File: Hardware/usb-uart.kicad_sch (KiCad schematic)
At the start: 16 parts, among them J3 USB_C_Receptacle_USB2.0, U6 SC4216H, U7 LTC4411

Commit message: added jumper to change the buck converter to 8.4v
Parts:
- C23: footprint Capacitor_SMD:C_0603_1608Metric -> Capacitor_SMD:C_0402_1005Metric
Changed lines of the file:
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@@
       (effects (font (size 1.27 1.27)) (justify left))
     )
-    (property "Footprint" "Capacitor_SMD:C_0603_1608Metric" (id 2) (at 262.89 105.41 0)
+    (property "Footprint" "Capacitor_SMD:C_0402_1005Metric" (id 2) (at 262.89 105.41 0)
       (effects (font (size 1.27 1.27)) hide)
     )

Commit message: End of V1
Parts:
- added C10, C9: 0.1uF, Capacitor_SMD:C_0603_1608Metric, symbol Device:C_Small
- added C18: 4.7uF, Capacitor_SMD:C_0603_1608Metric, symbol Device:C_Small
- added C8: 1.0uF, Capacitor_SMD:C_0603_1608Metric, symbol Device:C_Small
- added R17: 4.7k, Resistor_SMD:R_0603_1608Metric, symbol Device:R_Small
- added R3: 24k, Resistor_SMD:R_0603_1608Metric, symbol Device:R_Small
- added R6: 47k, Resistor_SMD:R_0603_1608Metric, symbol Device:R_Small
- added U3: INTERFACE-CP2102-GMR(QFN28), iclr:QFN28G_0.5-5X5MM, symbol iclr:INTERFACE-CP2102-GMR(QFN28)
- C23: footprint Capacitor_SMD:C_0402_1005Metric -> Capacitor_SMD:C_0603_1608Metric
- U6: value SC4216H -> RT9025-25GSP
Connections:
- net 3.3V: now also C10.2, C18.2, C8.2, C9.2, U3.6 (VDD), U3.7 (REGIN)
- net Data+: now also U3.4 (D+)
- net Data-: now also U3.5 (D-)
- net GND: now also C10.1, C18.1, C8.1, C9.1, R6.1, U3.3 (GND)
- net VBUS: now also R3.1
- new net: R3.2, R6.2, U3.8 (VBUS)
- new net: R17.2, U3.9 (~{RST})
- new net +3V3: R17.1
- new net DTR: U3.28 (DTR)
- new net RTS: U3.24 (RTS)
- new net RXD: U3.25 (RXD)
- new net TXD: U3.26 (TXD)
- no-connect marks 5 -> 23

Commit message: mostly completed v2 schematic (pin assignments left)
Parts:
- removed C10, C9: 0.1uF, Capacitor_SMD:C_0603_1608Metric, symbol Device:C_Small
- removed C18, C23: 4.7uF, Capacitor_SMD:C_0603_1608Metric, symbol Device:C_Small
- removed C20, C25: 10uF, Capacitor_SMD:C_0603_1608Metric, symbol Device:C_Small
- removed C8: 1.0uF, Capacitor_SMD:C_0603_1608Metric, symbol Device:C_Small
- removed R17: 4.7k, Resistor_SMD:R_0603_1608Metric, symbol Device:R_Small
- removed R24: 56k, Resistor_SMD:R_0603_1608Metric, symbol Device:R_Small
- removed R25: 10k, Resistor_SMD:R_0603_1608Metric, symbol Device:R_Small
- removed R3: 24k, Resistor_SMD:R_0603_1608Metric, symbol Device:R_Small
- removed R6: 47k, Resistor_SMD:R_0603_1608Metric, symbol Device:R_Small
- removed U3: INTERFACE-CP2102-GMR(QFN28), iclr:QFN28G_0.5-5X5MM, symbol iclr:INTERFACE-CP2102-GMR(QFN28)
- removed U6: RT9025-25GSP, iclr:SOIC127P599X175-9N, symbol iclr:RT9025-25GSP
- removed U7: LTC4411, Package_TO_SOT_SMD:SOT-23-5, symbol iclr:LTC4411
- R11: renamed from R15; footprint Resistor_SMD:R_0603_1608Metric -> Resistor_SMD:R_0402_1005Metric
- R12: renamed from R16; footprint Resistor_SMD:R_0603_1608Metric -> Resistor_SMD:R_0402_1005Metric
- R13: renamed from R18; footprint Resistor_SMD:R_0603_1608Metric -> Resistor_SMD:R_0402_1005Metric
- USBLED1: footprint LED_SMD:LED_0603_1608Metric -> Resistor_SMD:R_0402_1005Metric
- renumbered D4 to D2, J3 to J5, TP17 to TP1, TP18 to TP2, TP19 to TP3
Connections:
- no-connect marks 23 -> 2

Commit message: Mostly completed RBUS side, still buck converter side to do
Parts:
- removed TP3: TestPoint, TestPoint:TestPoint_Pad_D1.0mm, symbol Connector:TestPoint
- USBLED1: footprint Resistor_SMD:R_0402_1005Metric -> LED_SMD:LED_0402_1005Metric
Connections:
- net Data+: now also D2.2 (K); no longer D2.4 (K)
- net VBUS: now also D2.4 (K); no longer D2.2 (K)
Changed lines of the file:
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@@
-    (stroke (width 0) (type default) (color 0 0 0 0))
-  )
-  (wire (pts (xy 44.45 109.22) (xy 52.07 109.22))
     (stroke (width 0) (type default) (color 0 0 0 0))
   )
@@
     (stroke (width 0) (type default) (color 0 0 0 0))
   )
-  (label "Data+" (at 134.62 134.62 90)
-    (effects (font (size 1.27 1.27)) (justify left bottom))
-  )
-  (label "VBUS" (at 129.54 134.62 90)
+  (label "Data+" (at 129.54 134.62 90)
     (effects (font (size 1.27 1.27)) (justify left bottom))
   )
@@
     (effects (font (size 1.27 1.27)) (justify left bottom))
   )
+  (label "Data-" (at 132.08 134.62 90)
+    (effects (font (size 1.27 1.27)) (justify left bottom))
+  )
   (label "Data-" (at 44.45 99.06 0)
     (effects (font (size 1.27 1.27)) (justify left bottom))
   )
-  (label "Data-" (at 132.08 134.62 90)
-    (effects (font (size 1.27 1.27)) (justify left bottom))
-  )
   (label "Data-" (at 116.84 102.87 0)
     (effects (font (size 1.27 1.27)) (justify left bottom))
   )
-  (label "VBUS" (at 44.45 109.22 0)
-    (effects (font (size 1.27 1.27)) (justify left bottom))
-  )
   (label "Data+" (at 116.84 107.95 0)
+    (effects (font (size 1.27 1.27)) (justify left bottom))
+  )
+  (label "VBUS" (at 134.62 134.62 90)
     (effects (font (size 1.27 1.27)) (justify left bottom))
   )
@@
     (pin "1")
   )
-  (symbol (lib_id "Connector:TestPoint") (at 52.07 109.22 270) (unit 1)
-    (in_bom yes) (on_board yes)
-    (property "Reference" "TP3" (id 0) (at 56.8452 108.0516 90)
-      (effects (font (size 1.27 1.27)) (justify left))
-    )
-    (property "Value" "TestPoint" (id 1) (at 56.8452 110.363 90)
-      (effects (font (size 1.27 1.27)) (justify left))
-    )
-    (property "Footprint" "TestPoint:TestPoint_Pad_D1.0mm" (id 2) (at 52.07 114.3 0)
-      (effects (font (size 1.27 1.27)) hide)
-    )
-    (property "Datasheet" "~" (id 3) (at 52.07 114.3 0)
-      (effects (font (size 1.27 1.27)) hide)
-    )
-    (pin "1")
-  )
   (symbol (lib_id "Device:LED_Small") (at 162.56 92.71 180) (unit 1)
     (in_bom yes) (on_board yes)
     (property "Reference" "USBLED1" (id 0) (at 162.56 87.503 0))
     (property "Value" "USB_LED" (id 1) (at 162.56 89.8144 0))
-    (property "Footprint" "Resistor_SMD:R_0402_1005Metric" (id 2) (at 162.56 92.71 90)
-      (effects (font (size 1.27 1.27)) hide)
-    )
+    (property "Footprint" "LED_SMD:LED_0402_1005Metric" (id 2) (at 162.56 92.71 90)
+      (effects (font (size 1.27 1.27)) hide)
+    )

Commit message: new USB port, added 3d models for the taller connectors
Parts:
- J5: footprint Connector_USB:USB_C_Receptacle_GCT_USB4085 -> Connector_USB:USB_C_Receptacle_Palconn_UTC16-G
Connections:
- net Data+: now also D2.3 (K); no longer D2.2 (K)
- net Data-: now also D2.2 (K); no longer D2.3 (K)
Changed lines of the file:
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@@
     (stroke (width 0) (type default) (color 0 0 0 0))
-  )
-  (label "Data+" (at 129.54 134.62 90)
-    (effects (font (size 1.27 1.27)) (justify left bottom))
   )
   (label "Data+" (at 44.45 104.14 0)
     (effects (font (size 1.27 1.27)) (justify left bottom))
   )
-  (label "Data-" (at 132.08 134.62 90)
+  (label "Data+" (at 132.08 134.62 90)
     (effects (font (size 1.27 1.27)) (justify left bottom))
   )
@@
   )
   (label "VBUS" (at 134.62 134.62 90)
+    (effects (font (size 1.27 1.27)) (justify left bottom))
+  )
+  (label "Data-" (at 129.54 134.62 90)
     (effects (font (size 1.27 1.27)) (justify left bottom))
   )
@@
     (property "Reference" "J5" (id 0) (at 103.0478 82.1182 0))
     (property "Value" "USB_C_Receptacle_USB2.0" (id 1) (at 103.0478 84.4296 0))
-    (property "Footprint" "Connector_USB:USB_C_Receptacle_GCT_USB4085" (id 2) (at 104.14 104.14 0)
+    (property "Footprint" "Connector_USB:USB_C_Receptacle_Palconn_UTC16-G" (id 2) (at 104.14 104.14 0)
       (effects (font (size 1.27 1.27)) hide)
     )

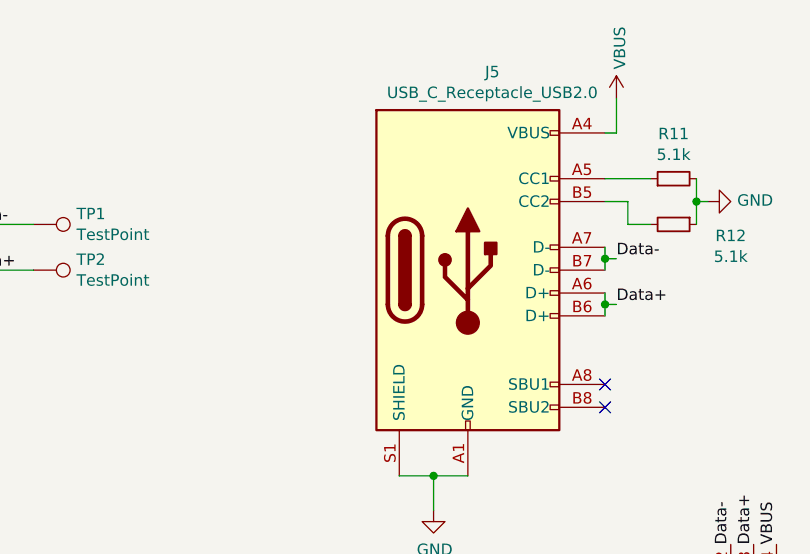
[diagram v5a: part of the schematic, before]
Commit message: on the verge of being complete, also updated to kicad 7
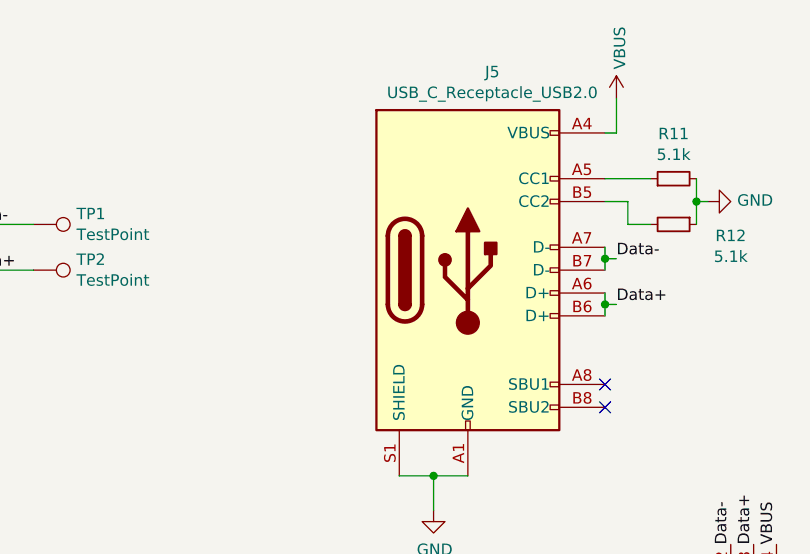
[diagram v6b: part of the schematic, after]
